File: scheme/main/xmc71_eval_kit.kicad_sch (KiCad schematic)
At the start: 0 parts

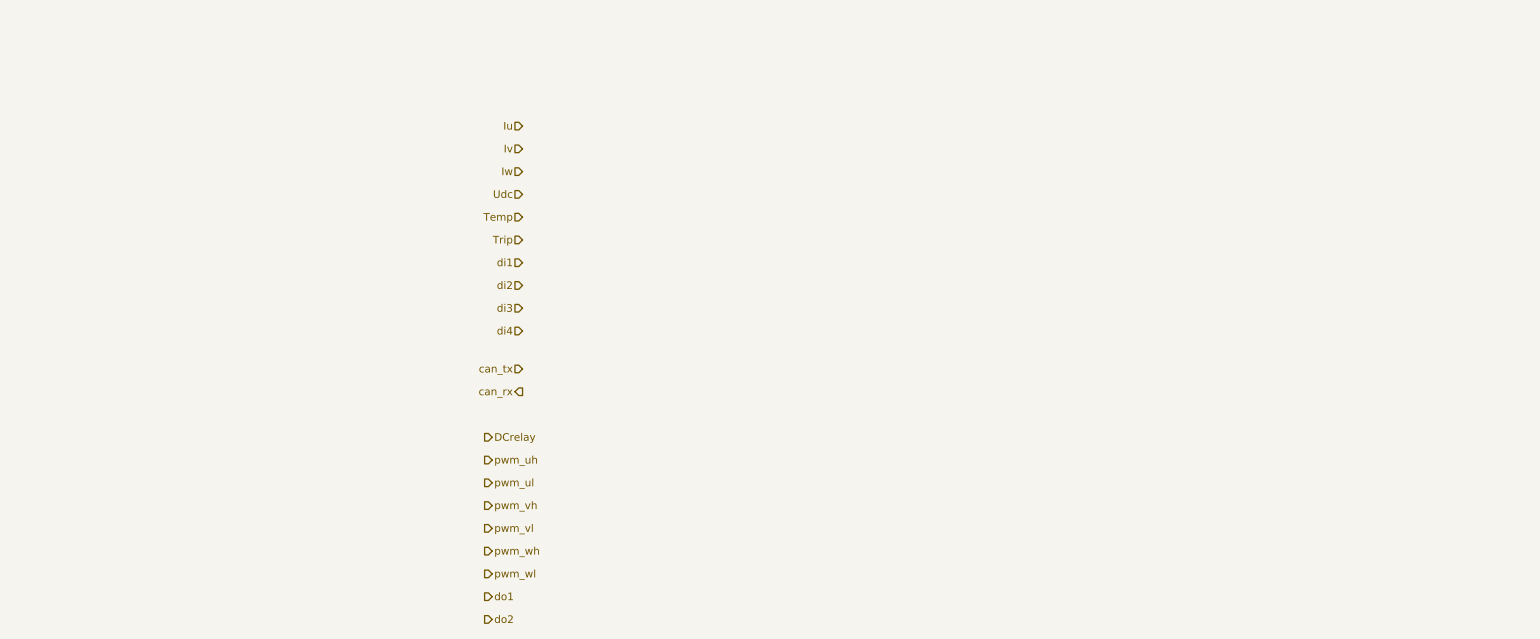
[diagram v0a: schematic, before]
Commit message: KIT_XMC71_EVK_LITE_V1 symbol
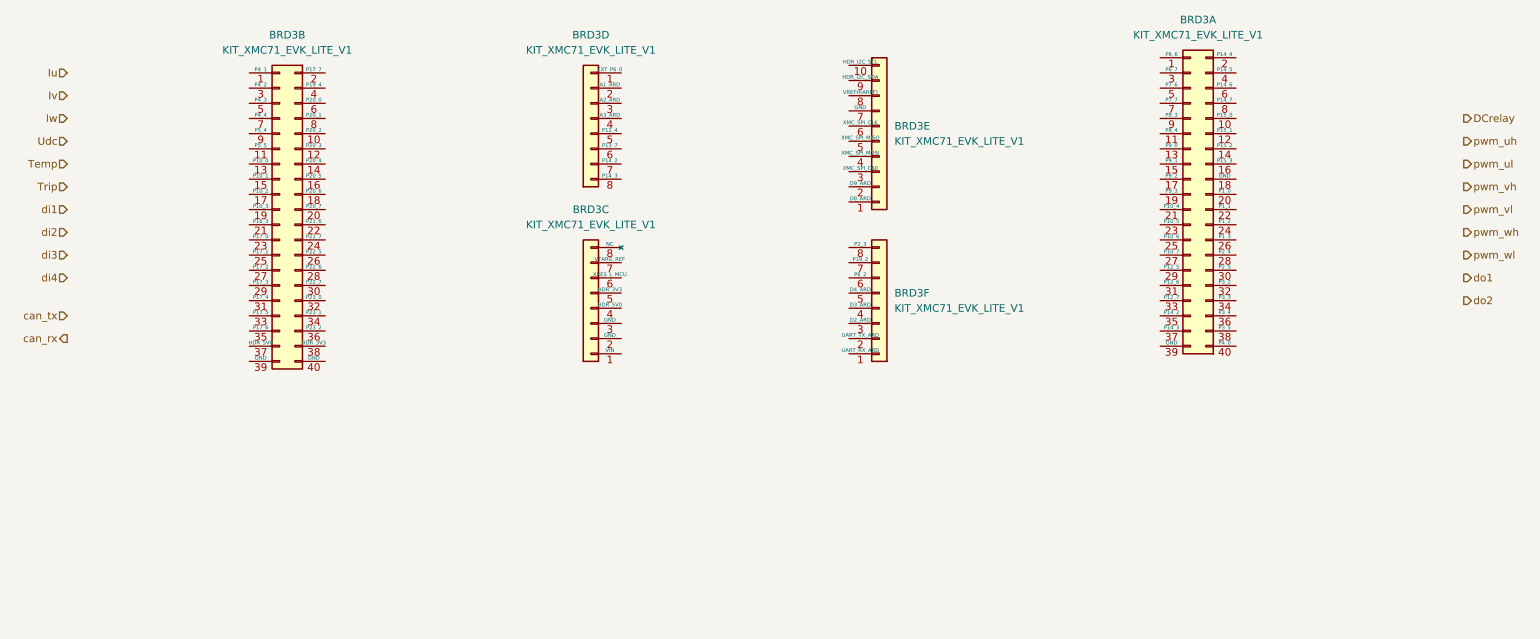
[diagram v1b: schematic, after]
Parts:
- added BRD3: KIT_XMC71_EVK_LITE_V1, symbol main:KIT_XMC71_EVK_LITE_V1
